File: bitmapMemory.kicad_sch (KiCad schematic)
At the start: 8 parts, among them U70 74LS245, U71 CY62256-70PC, U72 74LS244, U73 74LS244, U74 74LS244, U75 74LS244, U77 74LS244, U82 74LS244

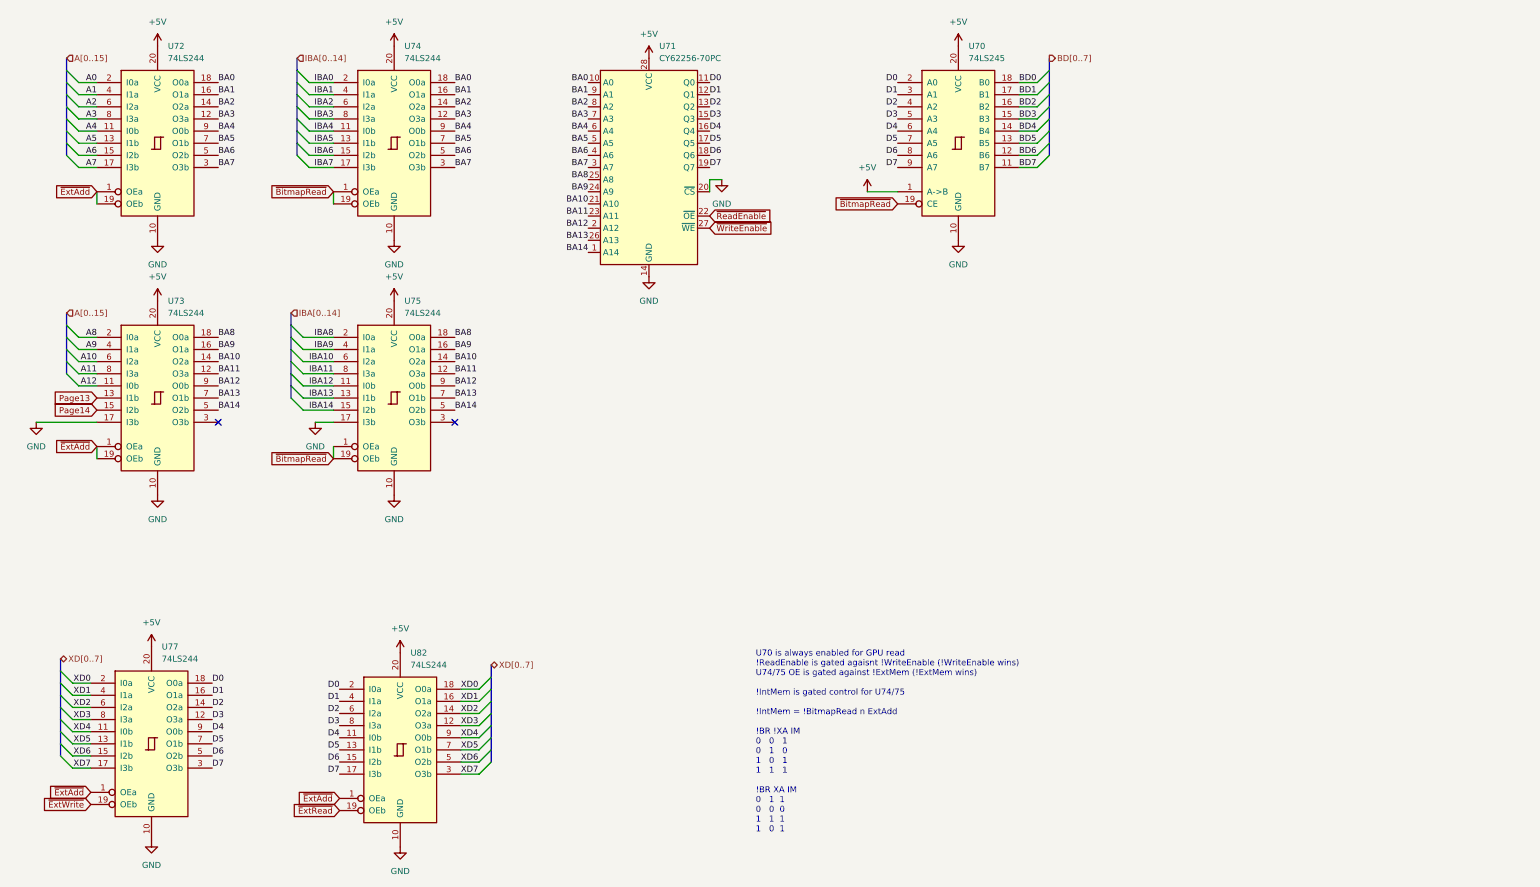
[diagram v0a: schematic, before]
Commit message: refine bus contention solution for host interface
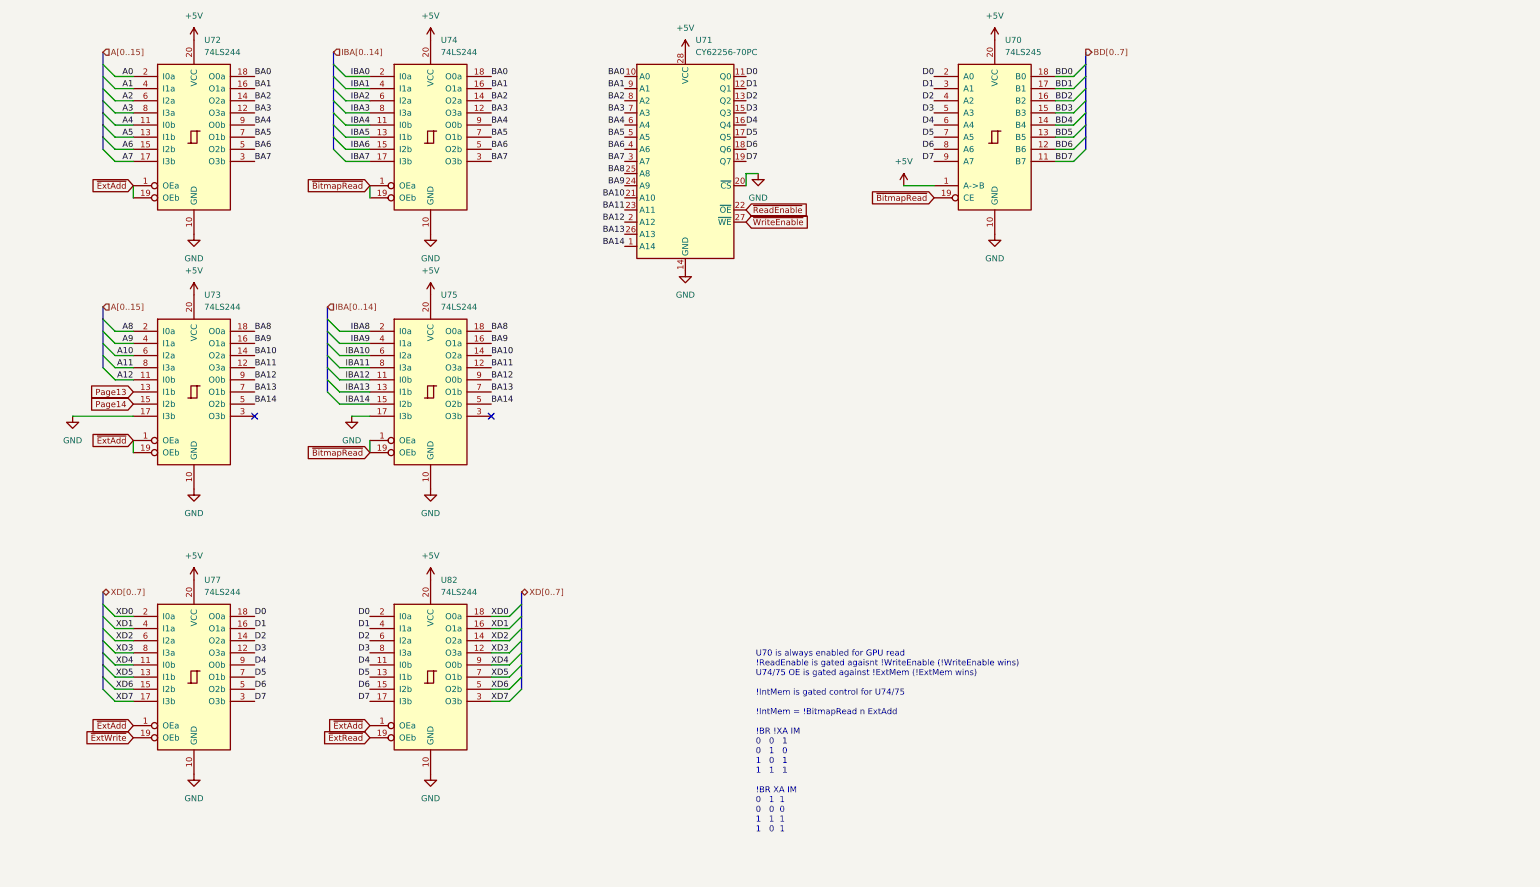
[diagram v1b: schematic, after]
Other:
- moved on the sheet: U70, U71, U72, U73, U74, U75, U77, U82

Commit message: tighten layout for final sizing
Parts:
- added C62, C63, C64, C65, C66, C67, C68, C69, C70: 10nF, Capacitor_SMD:C_0603_1608Metric, symbol Device:C_Small
- added C71: 4.7uF, Capacitor_SMD:CP_Elec_4x3, symbol Device:C_Polarized_Small
- added J2: Host Address Bus, Connector_PinHeader_2.54mm:PinHeader_1x16_P2.54mm_Vertical, symbol Connector_Generic:Conn_01x16
- added J54: BDBus, Connector_PinHeader_2.54mm:PinHeader_1x08_P2.54mm_Vertical, symbol Connector_Generic:Conn_01x08
- added J55: Power, Connector_PinSocket_2.54mm:PinSocket_1x04_P2.54mm_Vertical, symbol Connector_Generic:Conn_01x04
- added J56: XDBus, Connector_PinHeader_2.54mm:PinHeader_1x08_P2.54mm_Vertical, symbol Connector_Generic:Conn_01x08
- added J58: BitmapAddress, Connector_PinHeader_2.54mm:PinHeader_1x16_P2.54mm_Vertical, symbol Connector_Generic:Conn_01x16
- added J59: Control, Connector_PinHeader_2.54mm:PinHeader_1x08_P2.54mm_Vertical, symbol Connector_Generic:Conn_01x08
- added U137: 74LS08, Package_SO:SOIC-14_3.9x8.7mm_P1.27mm, symbol 74xx:74LS08
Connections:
- net ~{WriteEnable} is gone; now on net ~{ExtWrite}: U71.27 (~{WE})
- net +5V: now also C62.1, C63.1, C64.1, C65.1, C66.1, C67.1, C68.1, C69.1, C70.1, C71.1, J55.1 (Pin_1), J55.4 (Pin_4), U137.14 (VCC)
- net A0: now also J2.1 (Pin_1)
- net A1: now also U72.17 (I3b), J2.2 (Pin_2); no longer U72.4 (I1a)
- net A10: now also U73.15 (I2b), J2.11 (Pin_11); no longer U73.6 (I2a)
- net A11: now also U73.6 (I2a), J2.12 (Pin_12); no longer U73.8 (I3a)
- net A12: now also U73.13 (I1b), J2.13 (Pin_13); no longer U73.11 (I0b)
- net A2: now also U72.4 (I1a), J2.3 (Pin_3); no longer U72.6 (I2a)
- net A3: now also U72.6 (I2a), J2.4 (Pin_4); no longer U72.8 (I3a)
- net A4: now also U72.15 (I2b), J2.5 (Pin_5); no longer U72.11 (I0b)
- net A5: now also U72.8 (I3a), J2.6 (Pin_6); no longer U72.13 (I1b)
- net A6: now also U72.13 (I1b), J2.7 (Pin_7); no longer U72.15 (I2b)
- net A7: now also U72.11 (I0b), J2.8 (Pin_8); no longer U72.17 (I3b)
- net A8: now also J2.9 (Pin_9)
- net A9: now also J2.10 (Pin_10)
- net BA1: now also U72.3 (O3b), U74.3 (O3b); no longer U72.16 (O1a), U74.16 (O1a)
- net BA10: now also U73.5 (O2b), U75.16 (O1a); no longer U73.14 (O2a), U75.14 (O2a)
- net BA11: now also U73.14 (O2a), U75.7 (O1b); no longer U73.12 (O3a), U75.12 (O3a)
- net BA12: now also U73.7 (O1b), U75.14 (O2a); no longer U73.9 (O0b), U75.9 (O0b)
- net BA13: now also U73.12 (O3a), U75.9 (O0b); no longer U73.7 (O1b), U75.7 (O1b)
- net BA14: now also U73.9 (O0b), U75.12 (O3a); no longer U73.5 (O2b), U75.5 (O2b)
- net BA2: now also U72.16 (O1a), U74.16 (O1a); no longer U72.14 (O2a), U74.14 (O2a)
- net BA3: now also U72.14 (O2a), U74.5 (O2b); no longer U72.12 (O3a), U74.12 (O3a)
- net BA4: now also U72.5 (O2b), U74.14 (O2a); no longer U72.9 (O0b), U74.9 (O0b)
- net BA5: now also U72.12 (O3a); no longer U72.7 (O1b)
- net BA6: now also U72.7 (O1b), U74.12 (O3a); no longer U72.5 (O2b), U74.5 (O2b)
- net BA7: now also U72.9 (O0b), U74.9 (O0b); no longer U72.3 (O3b), U74.3 (O3b)
- net BA9: now also U75.5 (O2b); no longer U75.16 (O1a)
- net BD0: now also J54.1 (Pin_1)
- net BD1: now also J54.2 (Pin_2)
- net BD2: now also J54.3 (Pin_3)
- net BD3: now also J54.4 (Pin_4)
- net BD4: now also J54.5 (Pin_5)
- net BD5: now also J54.6 (Pin_6)
- net BD6: now also J54.7 (Pin_7)
- net BD7: now also J54.8 (Pin_8)
- net D0: now also U77.3 (O3b), U82.17 (I3b); no longer U77.18 (O0a), U82.2 (I0a)
- net D1: now also U77.18 (O0a), U82.2 (I0a); no longer U77.16 (O1a), U82.4 (I1a)
- net D2: now also U77.5 (O2b), U82.15 (I2b); no longer U77.14 (O2a), U82.6 (I2a)
- net D3: now also U77.16 (O1a), U82.4 (I1a); no longer U77.12 (O3a), U82.8 (I3a)
- net D4: now also U77.7 (O1b), U82.13 (I1b); no longer U77.9 (O0b), U82.11 (I0b)
- net D5: now also U77.14 (O2a), U82.6 (I2a); no longer U77.7 (O1b), U82.13 (I1b)
- net D6: now also U77.9 (O0b), U82.11 (I0b); no longer U77.5 (O2b), U82.15 (I2b)
- net D7: now also U77.12 (O3a), U82.8 (I3a); no longer U77.3 (O3b), U82.17 (I3b)
- net GND: now also C62.2, C63.2, C64.2, C65.2, C66.2, C67.2, C68.2, C69.2, C70.2, C71.2, J55.2 (Pin_2), J55.3 (Pin_3), U137.7 (GND)
- net IBA0: now also J58.1 (Pin_1)
- net IBA1: now also U74.17 (I3b), J58.2 (Pin_2); no longer U74.4 (I1a)
- net IBA10: now also U75.4 (I1a), J58.11 (Pin_11); no longer U75.6 (I2a)
- net IBA11: now also U75.13 (I1b), J58.12 (Pin_12); no longer U75.8 (I3a)
- net IBA12: now also U75.6 (I2a), J58.13 (Pin_13); no longer U75.11 (I0b)
- net IBA13: now also U75.11 (I0b), J58.14 (Pin_14); no longer U75.13 (I1b)
- net IBA14: now also U75.8 (I3a), J58.15 (Pin_15); no longer U75.15 (I2b)
- net IBA2: now also U74.4 (I1a), J58.3 (Pin_3); no longer U74.6 (I2a)
- net IBA3: now also U74.15 (I2b), J58.4 (Pin_4); no longer U74.8 (I3a)
- net IBA4: now also U74.6 (I2a), J58.5 (Pin_5); no longer U74.11 (I0b)
- net IBA5: now also J58.6 (Pin_6)
- net IBA6: now also U74.8 (I3a), J58.7 (Pin_7); no longer U74.15 (I2b)
- net IBA7: now also U74.11 (I0b), J58.8 (Pin_8); no longer U74.17 (I3b)
- net IBA8: now also J58.9 (Pin_9)
- net IBA9: now also U75.15 (I2b), J58.10 (Pin_10); no longer U75.4 (I1a)
- net Page13: now also U73.8 (I3a), J59.6 (Pin_6); no longer U73.13 (I1b)
- net Page14: now also U73.11 (I0b), J59.7 (Pin_7); no longer U73.15 (I2b)
- net XD0: now also U77.17 (I3b), U82.3 (O3b), J56.1 (Pin_1); no longer U77.2 (I0a), U82.18 (O0a)
- net XD1: now also U77.2 (I0a), U82.18 (O0a), J56.2 (Pin_2); no longer U77.4 (I1a), U82.16 (O1a)
- net XD2: now also U77.15 (I2b), U82.5 (O2b), J56.3 (Pin_3); no longer U77.6 (I2a), U82.14 (O2a)
- net XD3: now also U77.4 (I1a), U82.16 (O1a), J56.4 (Pin_4); no longer U77.8 (I3a), U82.12 (O3a)
- net XD4: now also U77.13 (I1b), U82.7 (O1b), J56.5 (Pin_5); no longer U77.11 (I0b), U82.9 (O0b)
- net XD5: now also U77.6 (I2a), U82.14 (O2a), J56.6 (Pin_6); no longer U77.13 (I1b), U82.7 (O1b)
- net XD6: now also U77.11 (I0b), U82.9 (O0b), J56.7 (Pin_7); no longer U77.15 (I2b), U82.5 (O2b)
- net XD7: now also U77.8 (I3a), U82.12 (O3a), J56.8 (Pin_8); no longer U77.17 (I3b), U82.3 (O3b)
- net ~{BitmapRead}: now also J59.3 (Pin_3), U137.5
- net ~{ExtAdd}: now also J59.2 (Pin_2)
- net ~{ExtRead}: now also J59.4 (Pin_4), U137.4
- net ~{ExtWrite}: now also J59.5 (Pin_5)
- net ~{ReadEnable}: now also U137.6
- new net A13: J2.14 (Pin_14)
- new net A14: J2.15 (Pin_15)
- new net A15: J2.16 (Pin_16)
- no-connect marks 2 -> 5
